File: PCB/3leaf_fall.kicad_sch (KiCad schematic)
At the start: 62 parts, among them J1 5034801600, J2 USB_C_Receptacle_USB2.0_16P, SW1 Switch, U1 HOLYIOT-18010-NRF52840, U3 BQ24075RGT, U4 XC6220B331MR

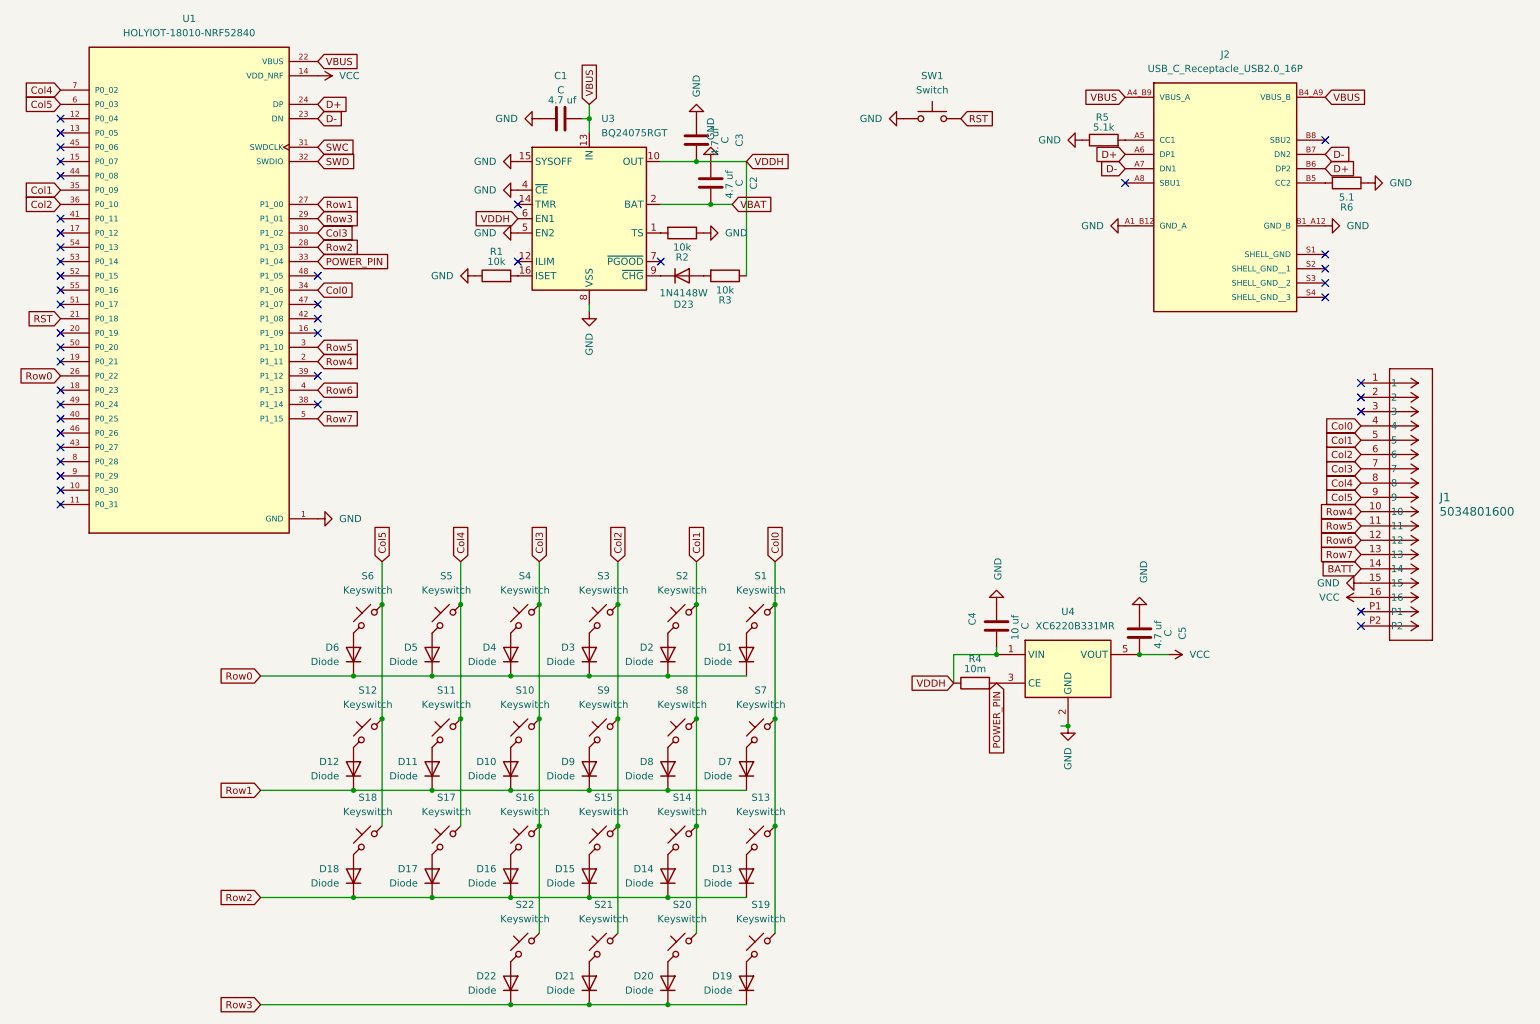
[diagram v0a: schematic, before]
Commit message: Near completion
* Updated switch footprint to meet PCB fab reqs
* Chose Raytac MDBT42 MCU
* Removed diodes
* Updated traces for diodeless config
* Added CR2032 battery contacts
* Removed USB board cutout

* More planning for battery mount
* Magnetic reed switch for power on/off
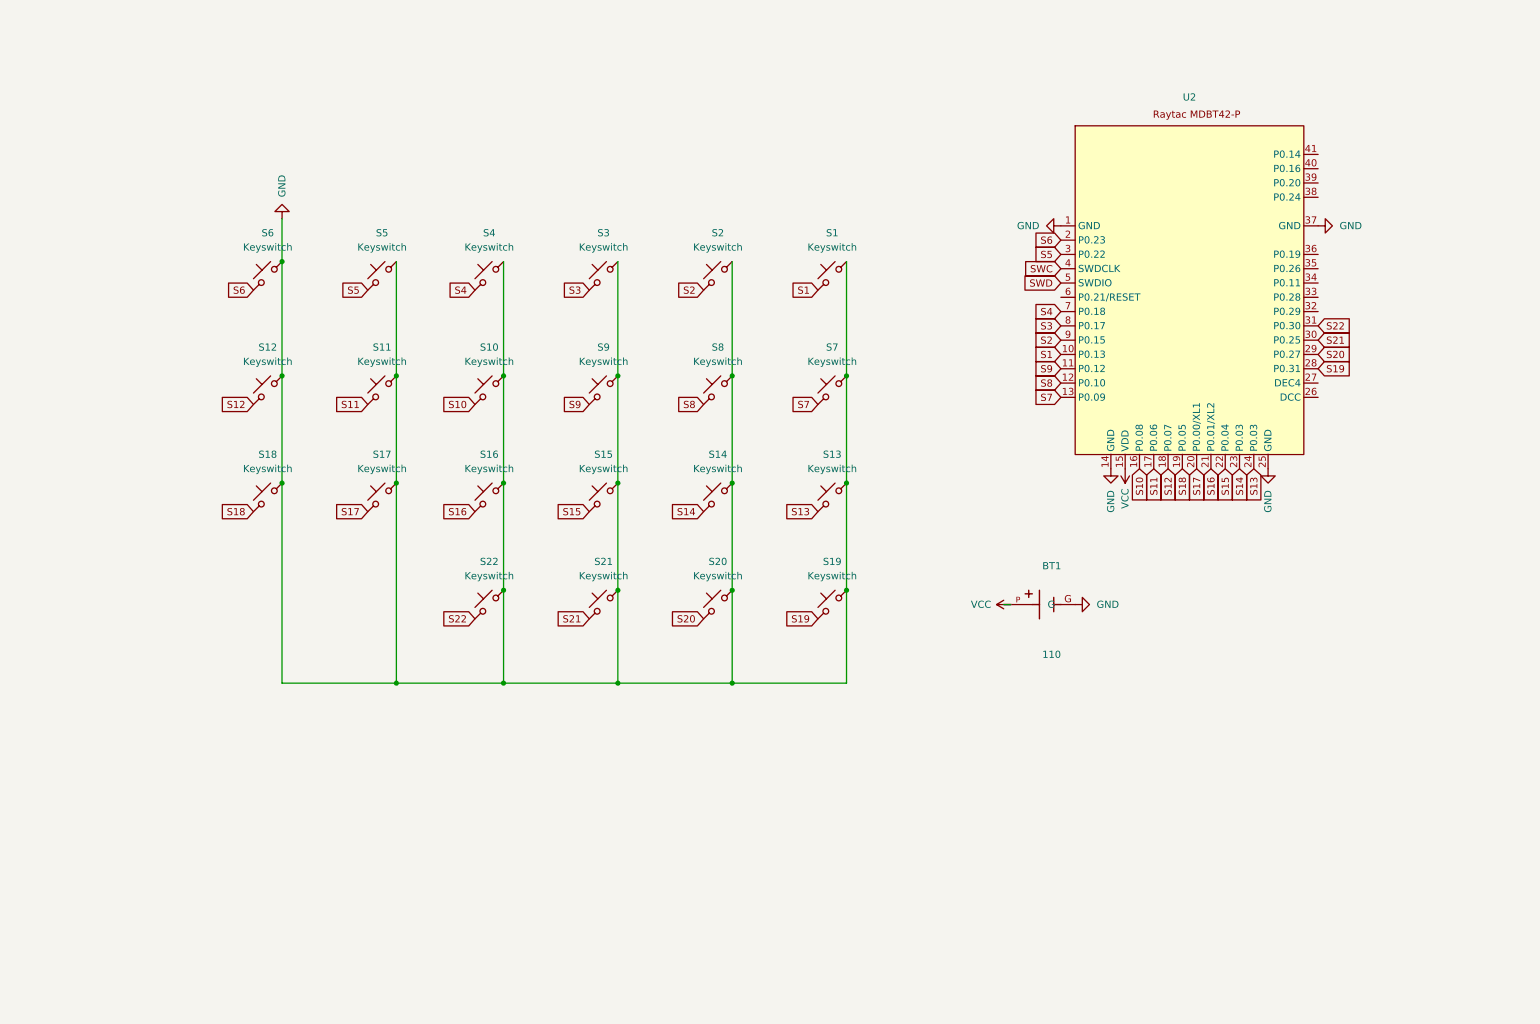
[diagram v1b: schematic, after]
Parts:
- removed C1, C2, C3, C4, C5: C, keeblib:C_0201_0603Metric, symbol Device:C
- removed D1, D10, D11, D12, D13, D14, D15, D16, D17, D18, D19, D2, D20, D21, D22, D3, D4, D5, D6, D7, D8, D9: Diode, Diode_SMD:D_SOD-323, symbol keeblib:Placeholder_Diode
- removed D23: 1N4148W, Diode_SMD:D_SOD-323, symbol Diode:1N4148W
- removed J1: 5034801600, keeblib:CON_5034801600_MOL, symbol keeblib:5034801600
- removed J2: USB_C_Receptacle_USB2.0_16P, keeblib:GCT_USB4500-03-1-A_REVA, symbol keeblib:USB4500-03-1-A_REVA
- removed R1, R2, R3: 10k, keeblib:R_0201_0603Metric, symbol Device:R
- removed R4: 10m, keeblib:R_0201_0603Metric, symbol Device:R
- removed R5: 5.1k, keeblib:R_0201_0603Metric, symbol Device:R
- removed R6: 5.1, keeblib:R_0201_0603Metric, symbol Device:R
- removed SW1: Switch, keeblib:EVQ_P7_PUC, symbol keeblib:Placeholder_Switch
- removed U1: HOLYIOT-18010-NRF52840, keeblib:XCVR_HOLYIOT-18010-NRF52840, symbol keeblib:HOLYIOT-18010-NRF52840
- removed U3: BQ24075RGT, Package_DFN_QFN:VQFN-16-1EP_3x3mm_P0.5mm_EP1.6x1.6mm, symbol Battery_Management:BQ24075RGT
- removed U4: XC6220B331MR, Package_TO_SOT_SMD:SOT-23-5, symbol Regulator_Linear:XC6220B331MR
- added BT1: 110, keeblib:BAT_110_2032, symbol keeblib:110
- added U2: ~, keeblib:Raytac_MDBT42, symbol keeblib:Raytac_MDBT42-P
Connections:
- net Col0 is gone; now on net GND: S1.1, S13.1, S19.1, S7.1
- net Col1 is gone; now on net GND: S14.1, S2.1, S20.1, S8.1
- net Col2 is gone; now on net GND: S15.1, S21.1, S3.1, S9.1
- net Col3 is gone; now on net GND: S10.1, S16.1, S22.1, S4.1
- net Col4 is gone; now on net GND: S11.1, S17.1, S5.1
- net Col5 is gone; now on net GND: S12.1, S18.1, S6.1
- net GND: now also BT1.G, U2.1 (GND), U2.14 (GND), U2.25 (GND), U2.37 (GND)
- net SWC: now also U2.4 (SWDCLK)
- net SWD: now also U2.5 (SWDIO)
- net VCC: now also BT1.P, U2.15 (VDD)
- net S2: now reaches S2.2
- net S2: now also U2.9 (P0.15)
- net S15: now reaches S15.2
- net S15: now also U2.22 (P0.04)
- net S14: now reaches S14.2
- net S14: now also U2.23 (P0.03)
- net S12: now reaches S12.2
- net S12: now also U2.18 (P0.07)
- net S6: now reaches S6.2
- net S6: now also U2.2 (P0.23)
- net S9: now reaches S9.2
- net S9: now also U2.11 (P0.12)
- net S1: now reaches S1.2
- net S1: now also U2.10 (P0.13)
- net S18: now reaches S18.2
- net S18: now also U2.19 (P0.05)
- net S20: now reaches S20.2
- net S20: now also U2.29 (P0.27)
- net S21: now reaches S21.2
- net S21: now also U2.30 (P0.25)
- net S10: now reaches S10.2
- net S10: now also U2.16 (P0.08)
- net S22: now reaches S22.2
- net S22: now also U2.31 (P0.30)
- net S11: now reaches S11.2
- net S11: now also U2.17 (P0.06)
- net S19: now reaches S19.2
- net S19: now also U2.28 (P0.31)
- net S16: now reaches S16.2
- net S16: now also U2.21 (P0.01/XL2)
- net S8: now reaches S8.2
- net S8: now also U2.12 (P0.10)
- net S17: now reaches S17.2
- net S17: now also U2.20 (P0.00/XL1)
- net S13: now reaches S13.2
- net S13: now also U2.24 (P0.03)
- net S5: now reaches S5.2
- net S5: now also U2.3 (P0.22)
- net S3: now reaches S3.2
- net S3: now also U2.8 (P0.17)
- net S7: now reaches S7.2
- net S7: now also U2.13 (P0.09)
- net S4: now reaches S4.2
- net S4: now also U2.7 (P0.18)
- no-connect marks 44 -> 0
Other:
- moved on the sheet: S1, S10, S11, S12, S13, S14, S15, S16, S17, S18, S19, S2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

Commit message: Add initial firmware, dongle
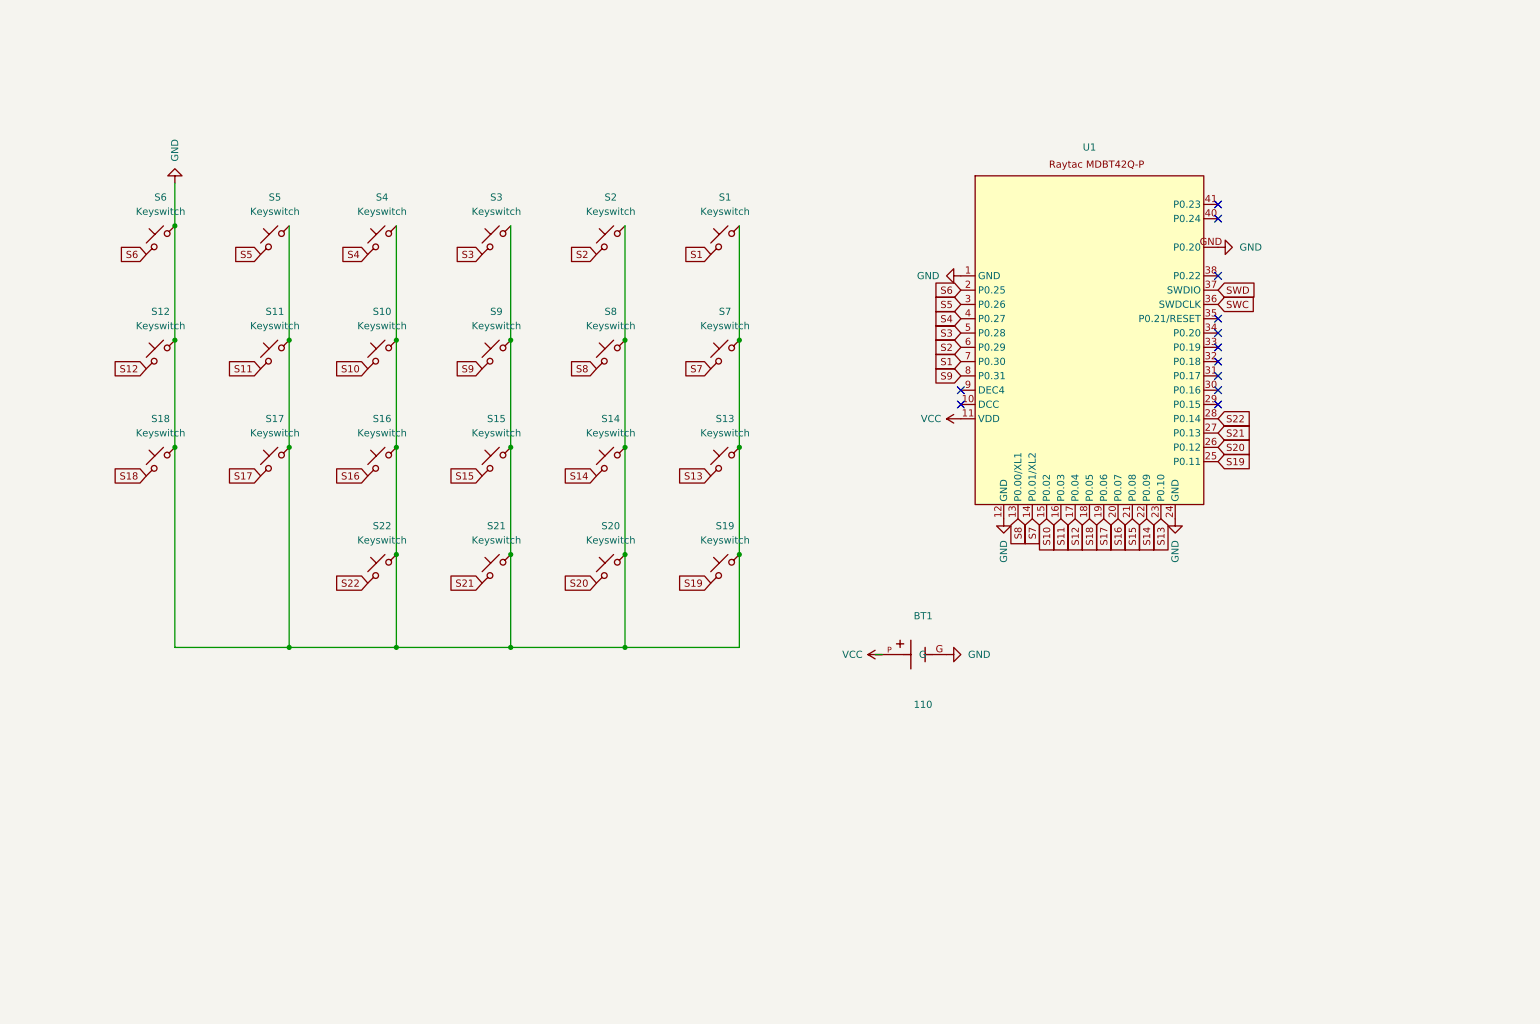
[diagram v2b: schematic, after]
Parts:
- removed U2: ~, keeblib:Raytac_MDBT42, symbol keeblib:Raytac_MDBT42-P
- added U1: (no value), keeblib:Raytac_MDBT42Q_P, symbol keeblib:Raytac_MDBT42Q-P
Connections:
- net GND: now also U1.1 (GND), U1.12 (GND), U1.24 (GND), U1.GND (P0.20)
- net S1: now also U1.7 (P0.30)
- net S10: now also U1.15 (P0.02)
- net S11: now also U1.16 (P0.03)
- net S12: now also U1.17 (P0.04)
- net S13: now also U1.23 (P0.10)
- net S14: now also U1.22 (P0.09)
- net S15: now also U1.21 (P0.08)
- net S16: now also U1.20 (P0.07)
- net S17: now also U1.19 (P0.06)
- net S18: now also U1.18 (P0.05)
- net S19: now also U1.25 (P0.11)
- net S2: now also U1.6 (P0.29)
- net S20: now also U1.26 (P0.12)
- net S21: now also U1.27 (P0.13)
- net S22: now also U1.28 (P0.14)
- net S3: now also U1.5 (P0.28)
- net S4: now also U1.4 (P0.27)
- net S5: now also U1.3 (P0.26)
- net S6: now also U1.2 (P0.25)
- net S7: now also U1.14 (P0.01/XL2)
- net S8: now also U1.13 (P0.00/XL1)
- net S9: now also U1.8 (P0.31)
- net SWC: now also U1.36 (SWDCLK)
- net SWD: now also U1.37 (SWDIO)
- net VCC: now also U1.11 (VDD)
- no-connect marks 0 -> 12
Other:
- moved on the sheet: BT1, S1, S10, S11, S12, S13, S14, S15, S16, S17, S18, S19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
